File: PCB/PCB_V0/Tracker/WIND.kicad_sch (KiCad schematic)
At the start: 22 parts, among them J3 Wind, Q1 BC337, U3 74HC123, U5 TL082

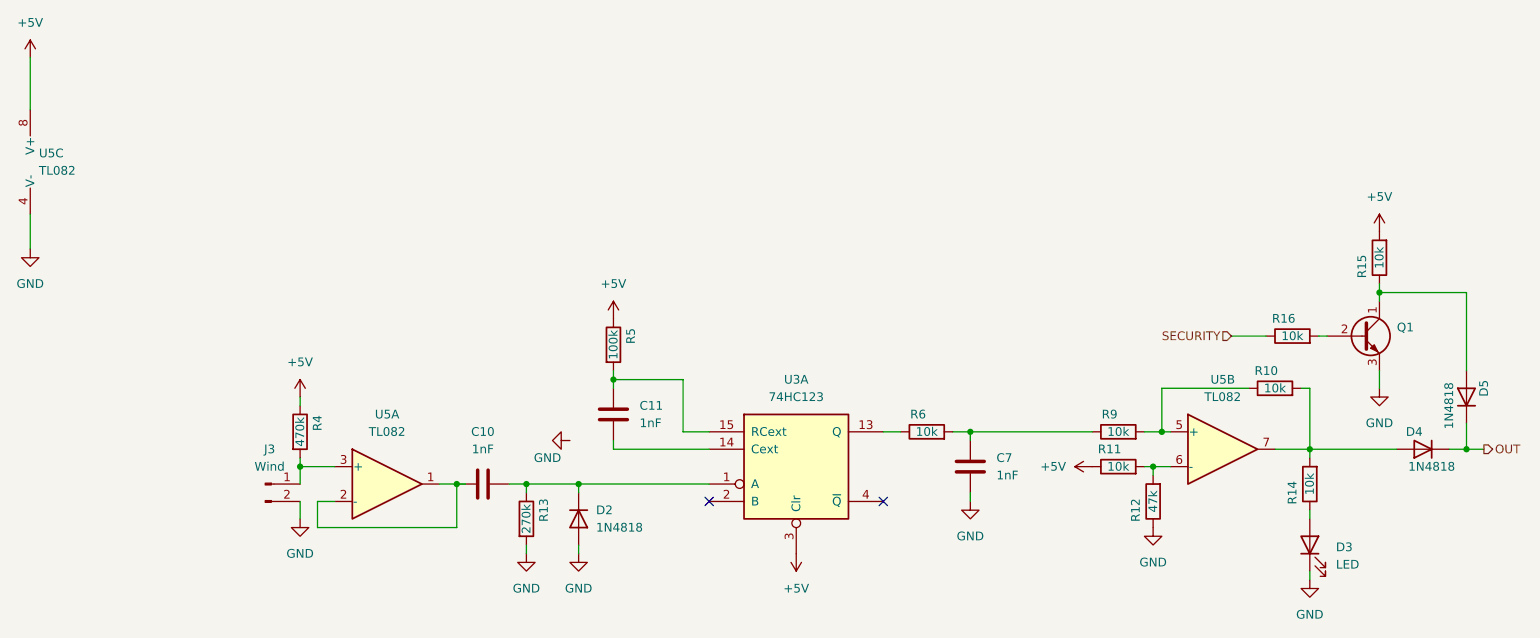
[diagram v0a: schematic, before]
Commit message: Add PCB with GNSS
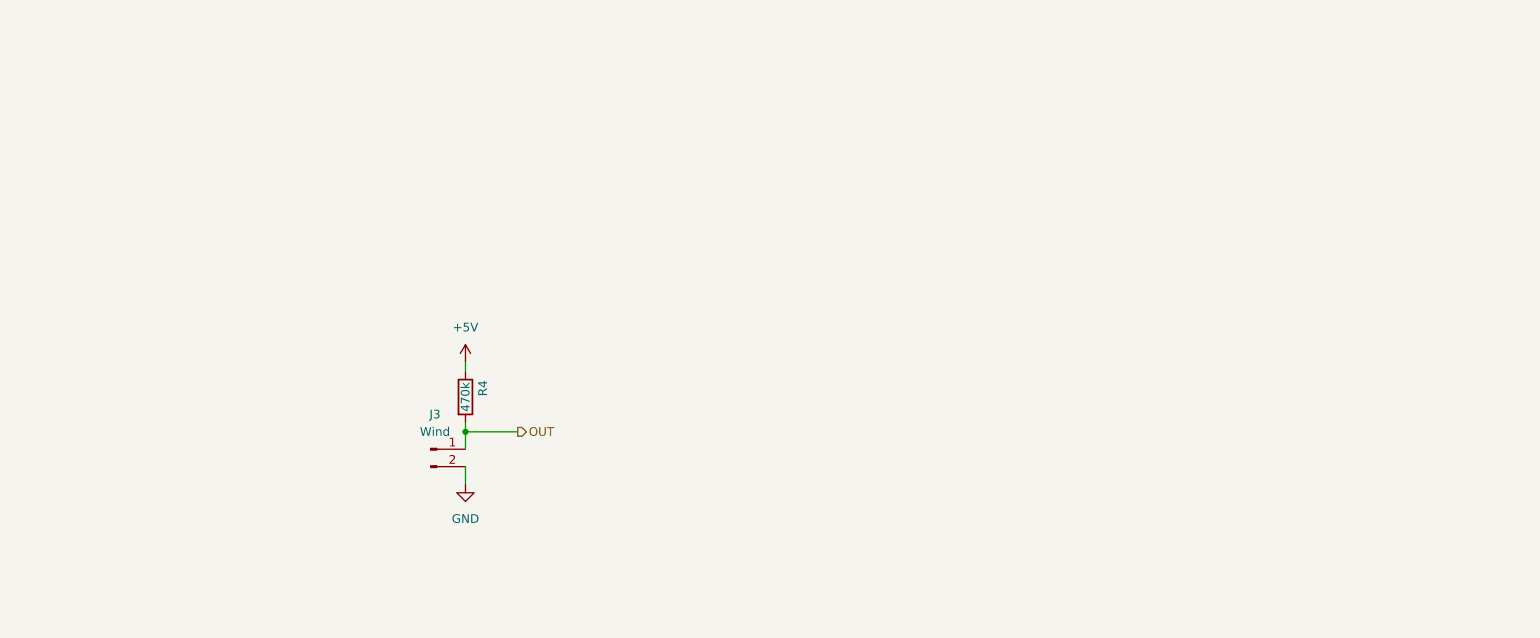
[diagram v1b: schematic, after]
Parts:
- removed C10, C11, C7: 1nF, Capacitor_THT:C_Rect_L7.0mm_W2.0mm_P5.00mm, symbol Device:C
- removed D2, D4, D5: 1N4818, Diode_THT:D_DO-41_SOD81_P7.62mm_Horizontal, symbol Device:D
- removed D3: LED, LED_THT:LED_D5.0mm, symbol Device:LED
- removed Q1: BC337, Package_TO_SOT_THT:TO-92_Inline, symbol Transistor_BJT:BC337
- removed R10, R11, R14, R15, R16, R6, R9: 10k, Resistor_THT:R_Axial_DIN0204_L3.6mm_D1.6mm_P5.08mm_Horizontal, symbol Device:R
- removed R12: 47k, Resistor_THT:R_Axial_DIN0204_L3.6mm_D1.6mm_P5.08mm_Horizontal, symbol Device:R
- removed R13: 270k, Resistor_THT:R_Axial_DIN0204_L3.6mm_D1.6mm_P5.08mm_Horizontal, symbol Device:R
- removed R5: 100k, Resistor_THT:R_Axial_DIN0204_L3.6mm_D1.6mm_P5.08mm_Horizontal, symbol Device:R
- removed U3: 74HC123, Package_DIP:DIP-16_W7.62mm, symbol 74xx:74HC123
- removed U5: TL082, Package_DIP:DIP-8_W7.62mm, symbol Amplifier_Operational:TL082
- J3: footprint Connector_Molex:Molex_KK-396_A-41791-0002_1x02_P3.96mm_Vertical -> TerminalBlock_Phoenix:TerminalBlock_Phoenix_MKDS-1,5-2-5.08_1x02_P5.08mm_Horizontal
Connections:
- net OUT: now also J3.1 (Pin_1), R4.2
- no-connect marks 2 -> 0
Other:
- moved on the sheet: J3, R4
